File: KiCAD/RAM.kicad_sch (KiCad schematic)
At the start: 16 parts

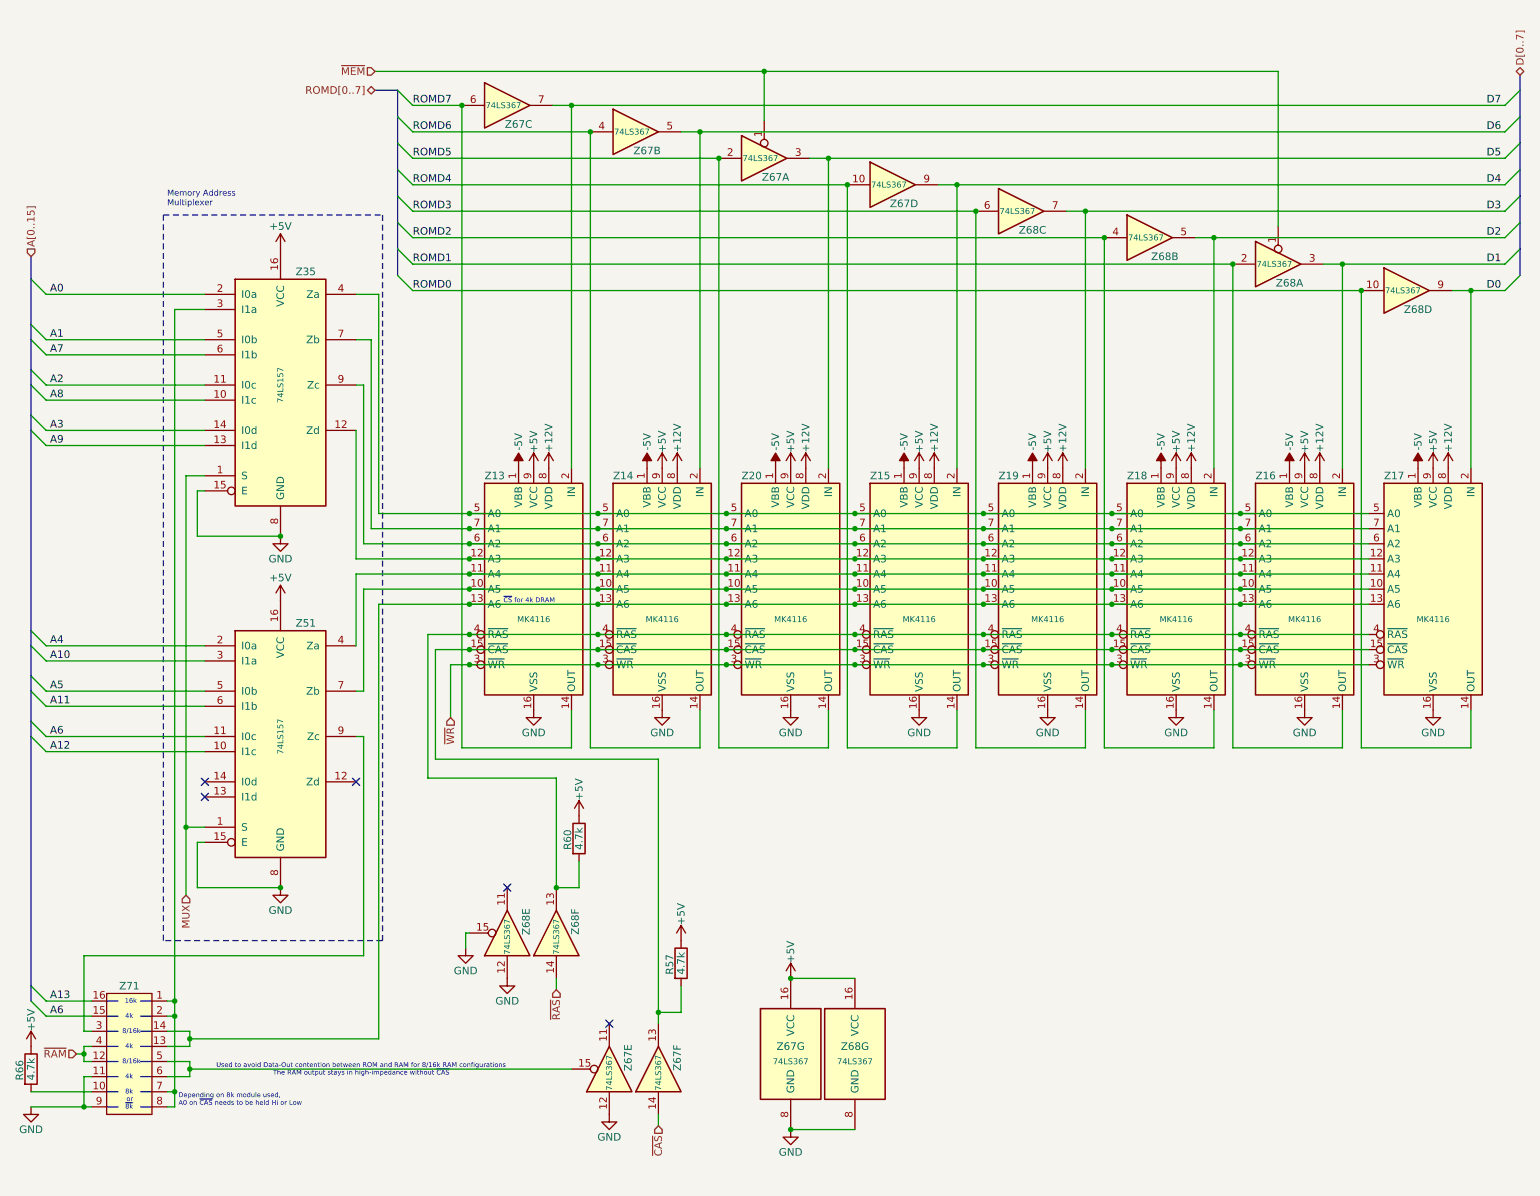
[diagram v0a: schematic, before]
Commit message: Update schematics (correct page flow) and add alternative to Q4 in BOM
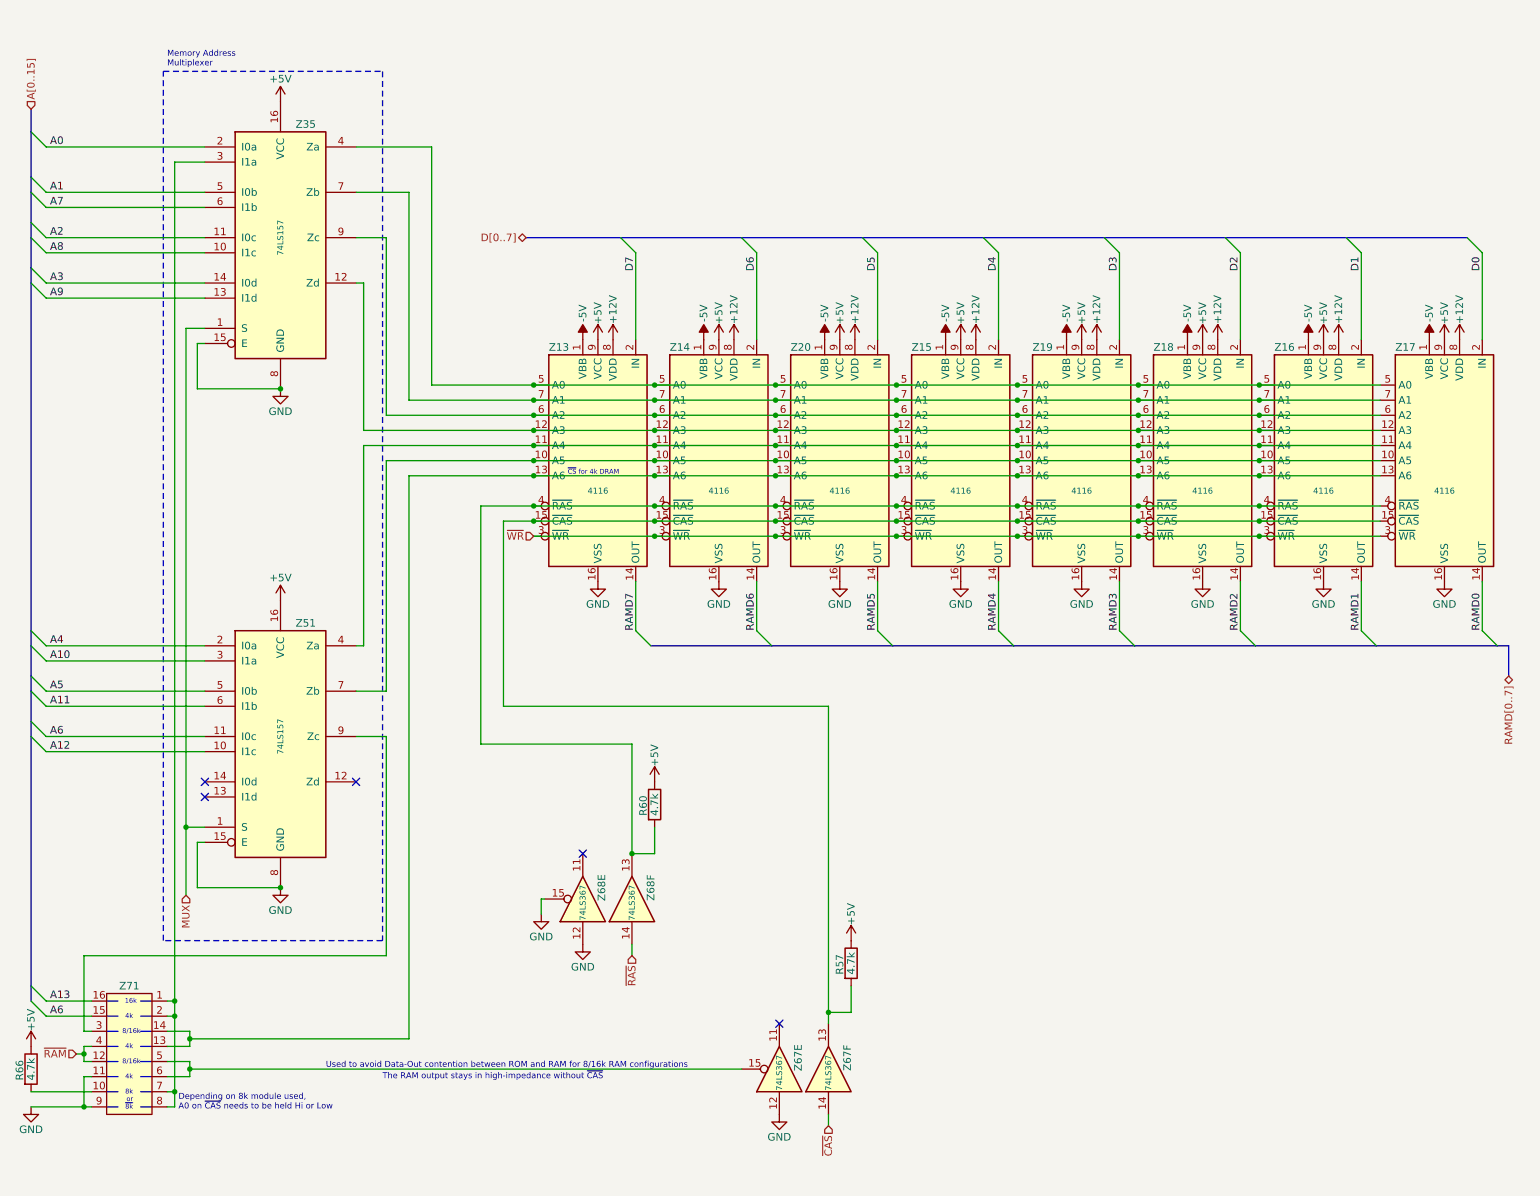
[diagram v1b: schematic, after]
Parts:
- removed unit 3 of Z67
- removed unit 2 of Z67
- removed unit 4 of Z67
- removed unit 7 of Z67
- removed unit 1 of Z67
- removed unit 1 of Z68
- removed unit 3 of Z68
- removed unit 4 of Z68
- removed unit 7 of Z68
- removed unit 2 of Z68
- Z13, Z14, Z15, Z16, Z17, Z18, Z19, Z20: value MK4116 -> 4116; footprint RetroStackLibrary:TRS80_Model_I_DIP16 -> Package_DIP:DIP-16_W7.62mm; symbol RetroStackLibrary:4116 -> RetroStackLibrary:DRAM_4116
- Z71: footprint RetroStackLibrary:TRS80_Model_I_DIP16 -> Package_DIP:DIP-16_W7.62mm; symbol RetroStackLibrary:TRS80ModelIX71 -> RetroStackLibrary:TRS80_Model_I_X71
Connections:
- net ROMD0 renamed RAMD0
- net ROMD1 renamed RAMD1
- net ROMD2 renamed RAMD2
- net ROMD3 renamed RAMD3
- net ROMD4 renamed RAMD4
- net ROMD5 renamed RAMD5
- net ROMD6 renamed RAMD6
- net ROMD7 renamed RAMD7
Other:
- moved on the sheet: R57, R60, Z13, Z14, Z15, Z16, Z17, Z18, Z19, Z20, Z35, Z67E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

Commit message: Updated revision to Rev C
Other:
- title: TRS-80 Model I G -> TRS-80 Model I Rev G
